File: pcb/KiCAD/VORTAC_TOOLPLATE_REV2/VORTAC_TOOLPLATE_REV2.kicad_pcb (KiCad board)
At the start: 4 copper layers, 12.2 x 17 mm, 9 parts, among them J1 Conn_01x07, J2 Conn_01x02, J4 Conn_01x02, J5 Conn_01x03

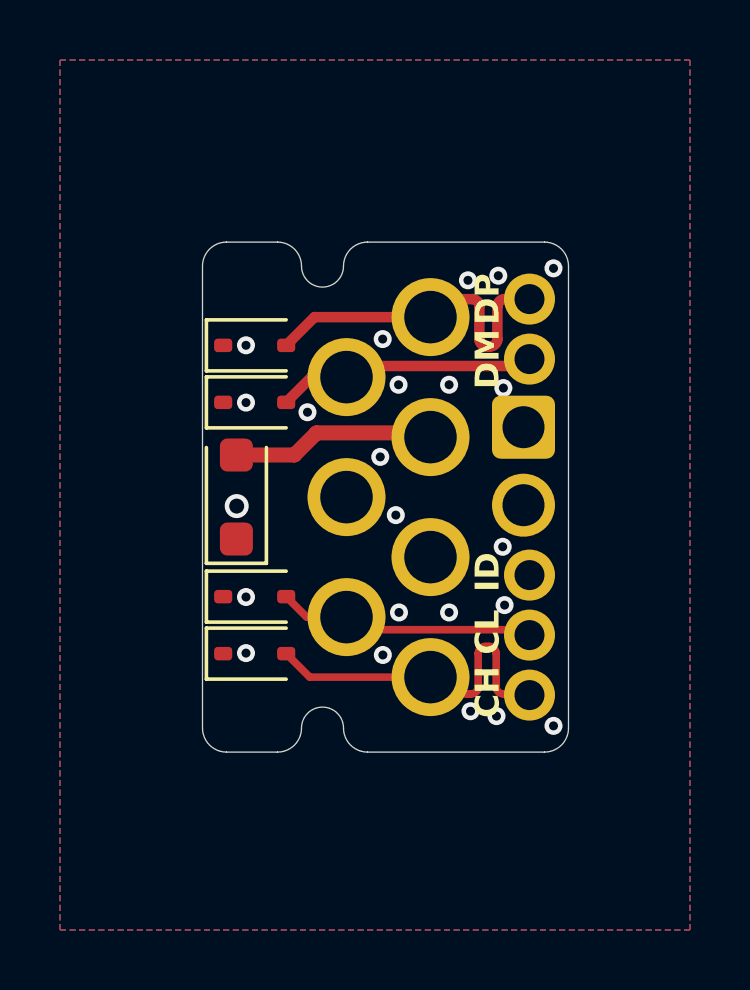
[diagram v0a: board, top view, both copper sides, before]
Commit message: (Hopefully) Finalized DOCK, TOOL and TOOLPLATE REV2 for ordering
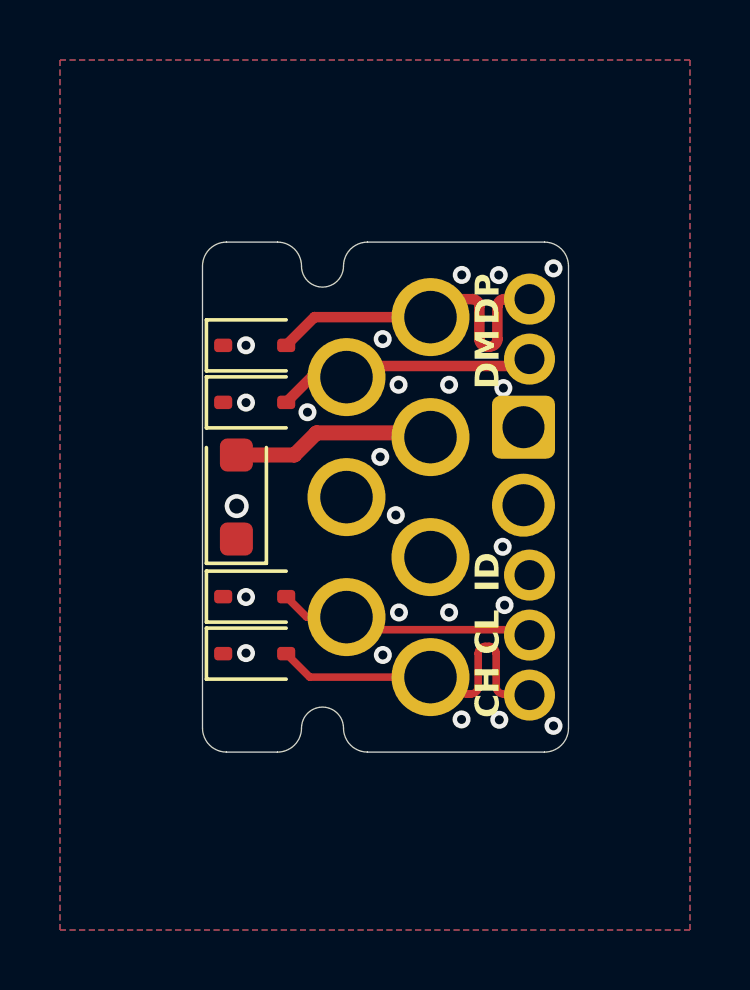
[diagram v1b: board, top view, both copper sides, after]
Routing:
- added copper zone on In1.Cu, net GND
- removed copper zone on In2.Cu, net GND
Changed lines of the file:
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@@
+	)
+	(gr_line
+		(start 107.8 91.499989)
+		(end 106.1 91.499989)
+		(stroke
+			(width 0.02)
+			(type default)
+		)
+		(layer "Edge.Cuts")
 	)
 	(gr_line
@@
 		(layer "Edge.Cuts")
 	)
+	(gr_arc
+		(start 110 92.299989)
+		(mid 109.3 92.999989)
+		(end 108.6 92.299989)
+		(stroke
+			(width 0.02)
+			(type default)
+		)
+		(layer "Edge.Cuts")
+	)
+	(gr_arc
+		(start 117.5 107.7)
+		(mid 117.265689 108.265682)
+		(end 116.696001 108.499989)
+		(stroke
+			(width 0.02)
+			(type default)
+		)
+		(layer "Edge.Cuts")
+	)
+	(gr_arc
+		(start 107.8 91.499989)
+		(mid 108.365689 91.734303)
+		(end 108.6 92.299989)
+		(stroke
+			(width 0.02)
+			(type default)
+		)
+		(layer "Edge.Cuts")
+	)
 	(gr_line
 		(start 107.796001 108.499989)
@@
 		(layer "Edge.Cuts")
 	)
+	(gr_arc
+		(start 110.8 108.499989)
+		(mid 110.234318 108.265674)
+		(end 110 107.699989)
+		(stroke
+			(width 0.02)
+			(type default)
+		)
+		(layer "Edge.Cuts")
+	)
 	(gr_line
-		(start 116.695805 108.499989)
-		(end 110.8 108.499989)
+		(start 116.7 91.499989)
+		(end 110.8 91.499989)
+		(stroke
+			(width 0.02)
+			(type default)
+		)
+		(layer "Edge.Cuts")
+	)
+	(gr_arc
+		(start 106.1 108.499989)
+		(mid 105.534318 108.265674)
+		(end 105.3 107.699989)
 		(stroke
 			(width 0.02)
@@
 		(layer "Edge.Cuts")
 	)
-	(gr_line
-		(start 106.1 91.5)
-		(end 106.1 91.499989)
+	(gr_arc
+		(start 105.3 92.3)
+		(mid 105.534318 91.734311)
+		(end 106.1 91.5)
 		(stroke
 			(width 0.02)
@@
 	)
 	(gr_arc
-		(start 110.8 108.499989)
-		(mid 110.234318 108.265674)
-		(end 110 107.699989)
-		(stroke
-			(width 0.02)
-			(type default)
-		)
-		(layer "Edge.Cuts")
-	)
-	(gr_arc
-		(start 110 92.299989)
-		(mid 109.3 92.999989)
-		(end 108.6 92.299989)
-		(stroke
-			(width 0.02)
-			(type default)
-		)
-		(layer "Edge.Cuts")
-	)
-	(gr_line
-		(start 105.3 92.3)
-		(end 105.3 107.699989)
-		(stroke
-			(width 0.02)
-			(type default)
-		)
-		(layer "Edge.Cuts")
-	)
-	(gr_arc
-		(start 107.8 91.499989)
-		(mid 108.365689 91.734303)
-		(end 108.6 92.299989)
-		(stroke
-			(width 0.02)
-			(type default)
-		)
-		(layer "Edge.Cuts")
-	)
-	(gr_arc
-		(start 117.5 107.7)
-		(mid 117.265689 108.265682)
-		(end 116.695805 108.499989)
-		(stroke
-			(width 0.02)
-			(type default)
-		)
-		(layer "Edge.Cuts")
-	)
-	(gr_arc
-		(start 106.1 108.499989)
-		(mid 105.534318 108.265674)
-		(end 105.3 107.699989)
-		(stroke
-			(width 0.02)
-			(type default)
-		)
-		(layer "Edge.Cuts")
-	)
-	(gr_line
-		(start 117.5 107.7)
-		(end 117.5 92.295805)
-		(stroke
-			(width 0.02)
-			(type default)
-		)
-		(layer "Edge.Cuts")
-	)
-	(gr_line
-		(start 107.8 91.499989)
-		(end 106.1 91.499989)
+		(start 108.6 107.699989)
+		(mid 108.365689 108.265682)
+		(end 107.796001 108.499989)
 		(stroke
 			(width 0.02)
@@
 		(layer "Edge.Cuts")
 	)
-	(gr_arc
+	(gr_line
+		(start 117.5 107.7)
+		(end 117.5 92.295805)
+		(stroke
+			(width 0.02)
+			(type default)
+		)
+		(layer "Edge.Cuts")
+	)
+	(gr_line
 		(start 105.3 92.3)
-		(mid 105.534318 91.734311)
-		(end 106.1 91.5)
-		(stroke
-			(width 0.02)
-			(type default)
-		)
-		(layer "Edge.Cuts")
-	)
-	(gr_arc
-		(start 108.6 107.699989)
-		(mid 108.365689 108.265682)
-		(end 107.796001 108.499989)
+		(end 105.3 107.699989)
 		(stroke
 			(width 0.02)
@@
 	)
 	(gr_line
-		(start 116.7 91.499989)
-		(end 110.8 91.499989)
+		(start 116.696001 108.499989)
+		(end 110.8 108.499989)
+		(stroke
+			(width 0.02)
+			(type default)
+		)
+		(layer "Edge.Cuts")
+	)
+	(gr_line
+		(start 106.1 91.5)
+		(end 106.1 91.499989)
 		(stroke
 			(width 0.02)
@@
 	)
 	(via
-		(at 114.148341 92.77356)
+		(at 113.941892 92.593952)
 		(size 0.6)
 		(drill 0.3)
@@
 	)
 	(via
-		(at 115.159998 92.619998)
+		(at 115.175873 92.599269)
 		(size 0.6)
 		(drill 0.3)
@@
 	)
 	(via
-		(at 114.233806 107.137)
+		(at 113.935328 107.410888)
 		(size 0.6)
 		(drill 0.3)
@@
 	)
 	(via
-		(at 115.1 107.3)
+		(at 115.193854 107.423211)
 		(size 0.6)
 		(drill 0.3)
@@
 	)
 	(segment
-		(start 110.1 100)
-		(end 113.12 100)
+		(start 113.093446 100)
+		(end 114.755168 101.661722)
 		(width 0.2)
-		(layer "In2.Cu")
+		(layer "In1.Cu")
 		(net 4)
 	)
 	(segment
-		(start 113.12 100)
-		(end 114.755168 101.635168)
-		(width 0.2)
-		(layer "In2.Cu")
-		(net 4)
-	)
-	(segment
-		(start 115.470897 102.6)
+		(start 115.46 102.6)
 		(end 116.2 102.6)
 		(width 0.2)
-		(layer "In2.Cu")
+		(layer "In1.Cu")
 		(net 4)
 	)
 	(segment
-		(start 114.755168 101.884271)
-		(end 115.470897 102.6)
+		(start 110.1 100)
+		(end 113.093446 100)
 		(width 0.2)
-		(layer "In2.Cu")
+		(layer "In1.Cu")
 		(net 4)
 	)
 	(segment
-		(start 114.755168 101.635168)
-		(end 114.755168 101.884271)
+		(start 114.755168 101.661722)
+		(end 114.755168 101.895168)
 		(width 0.2)
-		(layer "In2.Cu")
+		(layer "In1.Cu")
+		(net 4)
+	)
+	(segment
+		(start 114.755168 101.895168)
+		(end 115.46 102.6)
+		(width 0.2)
+		(layer "In1.Cu")
 		(net 4)
 	)
@@
 			(pts
 				(xy 100.55 85.43) (xy 121.55 85.43) (xy 121.55 114.43) (xy 100.55 114.43)
+			)
+		)
+	)
+	(zone
+		(net 3)
+		(net_name "GND")
+		(layer "In1.Cu")
+		(hatch edge 0.5)
+		(priority 2)
+		(connect_pads yes
+			(clearance 0.1)
+		)
+		(min_thickness 0.2)
+		(filled_areas_thickness no)
+		(fill yes
+			(thermal_gap 0.3)
+			(thermal_bridge_width 0.5)
+		)
+		(polygon
+			(pts
+				(xy 116.638461 102.838461) (xy 112.3 98.5) (xy 113.1 96.75) (xy 119.020496 98.55605) (xy 119.043545 89.97)
+				(xy 103.951527 89.97) (xy 103.962665 109.94) (xy 118.99 109.94) (xy 118.99 102.841449)
 			)
 		)
@@
 			(pts
 				(xy 101.55 86.43) (xy 122.55 86.43) (xy 122.55 115.43) (xy 101.55 115.43)
-			)
-		)
-	)
-	(zone
-		(net 3)
-		(net_name "GND")
-		(layer "In2.Cu")
-		(hatch edge 0.5)
-		(priority 2)
-		(connect_pads yes
-			(clearance 0.1)
-		)
-		(min_thickness 0.2)
-		(filled_areas_thickness no)
-		(fill yes
-			(thermal_gap 0.3)
-			(thermal_bridge_width 0.5)
-		)
-		(polygon
-			(pts
-				(xy 116.638461 102.838461) (xy 112.3 98.5) (xy 111 98.5) (xy 111 100.9) (xy 113.1 100.9) (xy 114.9 102.7)
-				(xy 115.108893 103.706653) (xy 115.586965 104.065206)
 			)
 		)
@@
 	)
 	(group ""
-		(members "170f173b-c503-4d18-8175-f05e1acbe481" "3f06e17e-eb80-4524-8479-404584fd4bf7"
-			"401b8d4e-2876-46a4-816f-be8e7cd33167" "43645ba7-3418-4df7-a265-03a1b084cc83"
-			"479f5196-869b-4c34-8286-0d5f7891b19d" "4c777764-e9a2-4d45-bf0e-5bfcee1a0cb3"
-			"5293640c-d2fe-4568-92fb-4639c1f4b7b6" "642d4bc6-38e7-43b6-bfeb-060fc27645b5"
-			"6a9b02f4-ed98-4f45-b104-9a8132dc9da0" "7b24e5bf-58bf-4aa4-b28b-1c7f9d82ab83"
-			"823222f2-b955-49c4-af08-d31fa80ae3e2" "8a270495-8da3-4e71-b493-d88bf58e55f0"
-			"c2779663-95be-4dd5-8eb0-3601bab518d2" "c7c03c8d-91d1-4a4a-a804-464ab79b68bf"
-			"d1683c6e-265c-4a65-844a-24f1dda24cc8" "d9cd4cea-6277-4ed5-acc1-b9a131786dce"
-			"e837cdf3-6a69-464e-abb7-90e0078b7ccb" "fa167ced-5945-4069-9498-f562faf71910"
-		)
-	)
+		(members "189be37c-3439-4850-b8db-6974f42d414d" "1eb32afd-c09a-49d3-ae12-d6a83744d406"
+			"21ee54d1-b25d-440f-a083-593e3c46dabb" "242c97c3-1370-4787-8902-4c74beb9e0d2"
+			"288aa2d1-6382-4c43-be0d-32008cc0b90d" "350e9400-8a52-413e-ae4d-a73dbf6f3c46"
+			"4d014e9c-20f1-44d2-99bb-bf8e222ef4f6" "50010738-3090-489a-8392-c9fe1120f1c0"
+			"674f5e72-4eab-41f2-b3bd-86c1b8f001f9" "8648dc25-1319-4131-a77e-5e9f68fa7bdf"
+			"86fe878b-47ff-46c9-addd-8170ecce94a7" "b0bccc83-bd2c-4986-b417-d6d081e2046a"
+			"b4405535-8cd3-40de-9a75-9224b159281d" "c09d0ece-3274-46aa-b816-d19768a841f7"
+			"c848ccdf-6681-411e-ad1a-b1265674c511" "d23981ec-fc30-452c-ad1c-a582f1353f26"
+			"eb2d2922-3a95-453e-a3d7-e5c4d8309672" "ef064b4e-5029-4913-86ad-a9a4b9f7b6c1"
+		)
+	)

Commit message: Production Files
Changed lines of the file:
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@@
 	(gr_line
 		(start 107.8 91.499989)
-		(end 106.1 91.499989)
-		(stroke
-			(width 0.02)
-			(type default)
-		)
-		(layer "Edge.Cuts")
-	)
-	(gr_line
-		(start 110.8 91.5)
-		(end 110.8 91.499989)
+		(end 106.1 91.5)
 		(stroke
 			(width 0.02)
@@
 	(gr_line
 		(start 116.7 91.499989)
-		(end 110.8 91.499989)
+		(end 110.8 91.5)
 		(stroke
 			(width 0.02)
@@
 		(start 116.696001 108.499989)
 		(end 110.8 108.499989)
-		(stroke
-			(width 0.02)
-			(type default)
-		)
-		(layer "Edge.Cuts")
-	)
-	(gr_line
-		(start 106.1 91.5)
-		(end 106.1 91.499989)
 		(stroke
 			(width 0.02)
@@
 	)
 	(group ""
-		(members "189be37c-3439-4850-b8db-6974f42d414d" "1eb32afd-c09a-49d3-ae12-d6a83744d406"
-			"21ee54d1-b25d-440f-a083-593e3c46dabb" "242c97c3-1370-4787-8902-4c74beb9e0d2"
-			"288aa2d1-6382-4c43-be0d-32008cc0b90d" "350e9400-8a52-413e-ae4d-a73dbf6f3c46"
-			"4d014e9c-20f1-44d2-99bb-bf8e222ef4f6" "50010738-3090-489a-8392-c9fe1120f1c0"
-			"674f5e72-4eab-41f2-b3bd-86c1b8f001f9" "8648dc25-1319-4131-a77e-5e9f68fa7bdf"
-			"86fe878b-47ff-46c9-addd-8170ecce94a7" "b0bccc83-bd2c-4986-b417-d6d081e2046a"
-			"b4405535-8cd3-40de-9a75-9224b159281d" "c09d0ece-3274-46aa-b816-d19768a841f7"
-			"c848ccdf-6681-411e-ad1a-b1265674c511" "d23981ec-fc30-452c-ad1c-a582f1353f26"
-			"eb2d2922-3a95-453e-a3d7-e5c4d8309672" "ef064b4e-5029-4913-86ad-a9a4b9f7b6c1"
-		)
-	)
+		(members "189be37c-3439-4850-b8db-6974f42d414d" "21ee54d1-b25d-440f-a083-593e3c46dabb"
+			"242c97c3-1370-4787-8902-4c74beb9e0d2" "288aa2d1-6382-4c43-be0d-32008cc0b90d"
+			"350e9400-8a52-413e-ae4d-a73dbf6f3c46" "4d014e9c-20f1-44d2-99bb-bf8e222ef4f6"
+			"50010738-3090-489a-8392-c9fe1120f1c0" "674f5e72-4eab-41f2-b3bd-86c1b8f001f9"
+			"8648dc25-1319-4131-a77e-5e9f68fa7bdf" "86fe878b-47ff-46c9-addd-8170ecce94a7"
+			"b0bccc83-bd2c-4986-b417-d6d081e2046a" "b4405535-8cd3-40de-9a75-9224b159281d"
+			"c09d0ece-3274-46aa-b816-d19768a841f7" "c848ccdf-6681-411e-ad1a-b1265674c511"
+			"d23981ec-fc30-452c-ad1c-a582f1353f26" "eb2d2922-3a95-453e-a3d7-e5c4d8309672"
+		)
+	)
